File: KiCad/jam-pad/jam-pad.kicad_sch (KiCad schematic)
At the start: 80 parts, among them J1 USB_C, J2 PH_01x03_2.54mm, SW1 MX_Hotswap_LED_RGB, SW13 SW_Push, SW14 RotaryEncoder_Switch, SW15 SW_Push, SW2 MX_Hotswap_LED_RGB, SW3 MX_Hotswap_LED_RGB, SW4 MX_Hotswap_LED_RGB, SW5 MX_Hotswap_LED_RGB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

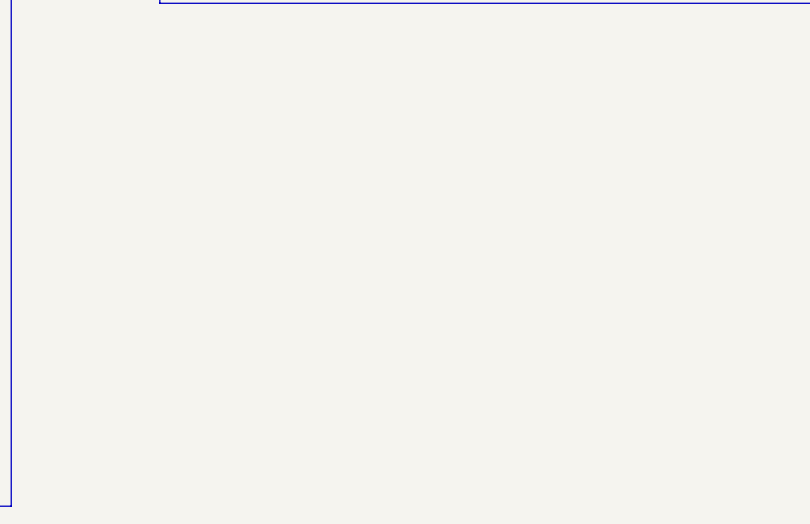
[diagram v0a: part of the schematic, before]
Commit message: Remove unconnected tracks and pass schematic parity
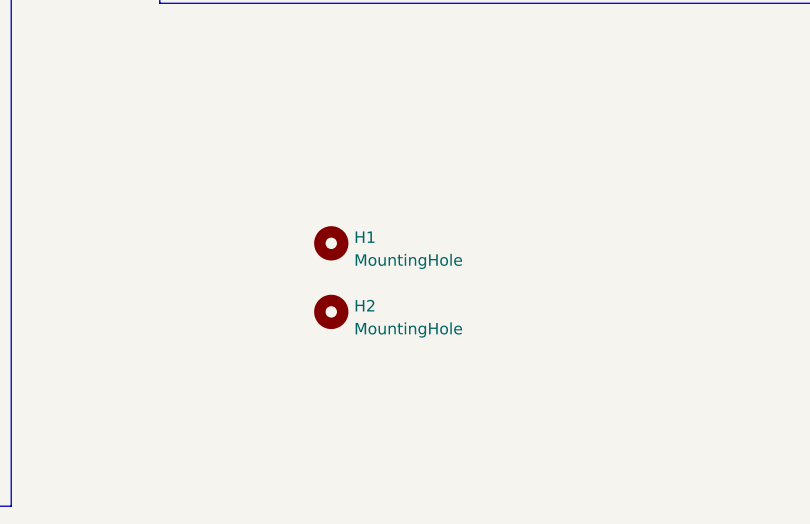
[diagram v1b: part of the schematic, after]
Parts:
- added H1, H2: MountingHole, MountingHole:MountingHole_2.2mm_M2_Pad, symbol Mechanical:MountingHole
- U1: footprint jam-pad:RP2040-QFN-56_HandSoldering -> jam-pad:RP2040-QFN-56
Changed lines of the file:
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@@
       (effects (font (size 1.27 1.27)))
     )
-    (property "Footprint" "jam-pad:RP2040-QFN-56_HandSoldering" (at 322.58 119.38 0)
+    (property "Footprint" "jam-pad:RP2040-QFN-56" (at 322.58 119.38 0)
       (effects (font (size 1.27 1.27)) hide)
     )
@@
     )
   )
+  (symbol (lib_id "Mechanical:MountingHole") (at 284.48 228.6 0) (unit 1)
+    (in_bom no) (on_board yes) (dnp no) (fields_autoplaced)
+    (property "Reference" "H2" (at 287.02 227.965 0)
+      (effects (font (size 1.27 1.27)) (justify left))
+    )
+    (property "Value" "MountingHole" (at 287.02 230.505 0)
+      (effects (font (size 1.27 1.27)) (justify left))
+    )
+    (property "Footprint" "MountingHole:MountingHole_2.2mm_M2_Pad" (at 284.48 228.6 0)
+      (effects (font (size 1.27 1.27)) hide)
+    )
+    (property "Datasheet" "~" (at 284.48 228.6 0)
+      (effects (font (size 1.27 1.27)) hide)
+    )
+    (property "JLCPCB_IGNORE" "Y" (at 284.48 228.6 0)
+      (effects (font (size 1.27 1.27)) hide)
+    )
+    (instances
+      (project "jam-pad"
+        (path "/1926255f-b0ba-44f2-aedc-792e85134e40"
+          (reference "H2") (unit 1)
+        )
+      )
+    )
+  )
   (symbol (lib_id "power:GND") (at 273.05 124.46 270) (unit 1)
     (in_bom yes) (on_board yes) (dnp no)
@@
         )
       )
+    )
+  )
+  (symbol (lib_id "Mechanical:MountingHole") (at 284.48 220.98 0) (unit 1)
+    (in_bom no) (on_board yes) (dnp no) (fields_autoplaced)
+    (property "Reference" "H1" (at 287.02 220.345 0)
+      (effects (font (size 1.27 1.27)) (justify left))
+    )
+    (property "Value" "MountingHole" (at 287.02 222.885 0)
+      (effects (font (size 1.27 1.27)) (justify left))
+    )
+    (property "Footprint" "MountingHole:MountingHole_2.2mm_M2_Pad" (at 284.48 220.98 0)
+      (effects (font (size 1.27 1.27)) hide)
+    )
+    (property "Datasheet" "~" (at 284.48 220.98 0)
+      (effects (font (size 1.27 1.27)) hide)
+    )
+    (property "JLCPCB_IGNORE" "Y" (at 284.48 220.98 0)
+      (effects (font (size 1.27 1.27)) hide)
+    )
+    (instances
+      (project "jam-pad"
+        (path "/1926255f-b0ba-44f2-aedc-792e85134e40"
+          (reference "H1") (unit 1)
+        )
+      )

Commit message: fab, clover logo, some other stuff? idr sorry
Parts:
- SW1, SW2, SW3, SW4, SW5, SW6, SW7, SW8, SW9, Y1: JLCPCB_IGNORE (none) -> Y
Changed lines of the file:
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@@
       (effects (font (size 1.27 1.27)) hide)
     )
+    (property "JLCPCB_IGNORE" "Y" (at 156.21 107.95 0)
+      (effects (font (size 1.27 1.27)) hide)
+    )
     (pin "1")
     (pin "2")
@@
       (effects (font (size 1.27 1.27)) hide)
     )
+    (property "JLCPCB_IGNORE" "Y" (at 156.21 120.65 0)
+      (effects (font (size 1.27 1.27)) hide)
+    )
     (pin "1")
     (pin "2")
@@
       (effects (font (size 1.27 1.27)) hide)
     )
+    (property "JLCPCB_IGNORE" "Y" (at 243.84 144.145 0)
+      (effects (font (size 1.27 1.27)) hide)
+    )
     (pin "1")
     (pin "2")
@@
       (effects (font (size 1.27 1.27)) hide)
     )
+    (property "JLCPCB_IGNORE" "Y" (at 181.61 107.95 0)
+      (effects (font (size 1.27 1.27)) hide)
+    )
     (pin "1")
     (pin "2")
@@
       (effects (font (size 1.27 1.27)) hide)
     )
+    (property "JLCPCB_IGNORE" "Y" (at 167.64 144.145 0)
+      (effects (font (size 1.27 1.27)) hide)
+    )
     (pin "1")
     (pin "2")
@@
       (effects (font (size 1.27 1.27)) hide)
     )
+    (property "JLCPCB_IGNORE" "Y" (at 121.92 144.145 0)
+      (effects (font (size 1.27 1.27)) hide)
+    )
     (pin "1")
     (pin "2")
@@
       (effects (font (size 1.27 1.27)) hide)
     )
+    (property "JLCPCB_IGNORE" "Y" (at 152.4 144.145 0)
+      (effects (font (size 1.27 1.27)) hide)
+    )
     (pin "1")
     (pin "2")
@@
       (effects (font (size 1.27 1.27)) hide)
     )
+    (property "JLCPCB_IGNORE" "Y" (at 181.61 95.25 0)
+      (effects (font (size 1.27 1.27)) hide)
+    )
     (pin "1")
     (pin "2")
@@
       (effects (font (size 1.27 1.27)) hide)
     )
+    (property "JLCPCB_IGNORE" "Y" (at 182.88 144.145 0)
+      (effects (font (size 1.27 1.27)) hide)
+    )
     (pin "1")
     (pin "2")
@@
       (effects (font (size 1.27 1.27)) hide)
     )
+    (property "JLCPCB_IGNORE" "Y" (at 228.6 144.145 0)
+      (effects (font (size 1.27 1.27)) hide)
+    )
     (pin "1")
     (pin "2")
@@
       (effects (font (size 1.27 1.27)) hide)
     )
+    (property "JLCPCB_IGNORE" "Y" (at 213.36 144.145 0)
+      (effects (font (size 1.27 1.27)) hide)
+    )
     (pin "1")
     (pin "2")
@@
       (effects (font (size 1.27 1.27)) hide)
     )
+    (property "JLCPCB_IGNORE" "Y" (at 285.75 124.46 0)
+      (effects (font (size 1.27 1.27)) hide)
+    )
     (pin "1")
     (pin "2")
@@
       (effects (font (size 1.27 1.27)) hide)
     )
+    (property "JLCPCB_IGNORE" "Y" (at 156.21 95.25 0)
+      (effects (font (size 1.27 1.27)) hide)
+    )
     (pin "1")
     (pin "2")
@@
       (effects (font (size 1.27 1.27)) hide)
     )
+    (property "JLCPCB_IGNORE" "Y" (at 198.12 144.145 0)
+      (effects (font (size 1.27 1.27)) hide)
+    )
     (pin "1")
     (pin "2")
@@
       (effects (font (size 1.27 1.27)) hide)
     )
+    (property "JLCPCB_IGNORE" "Y" (at 181.61 120.65 0)
+      (effects (font (size 1.27 1.27)) hide)
+    )
     (pin "1")
     (pin "2")
@@
       (effects (font (size 1.27 1.27)) hide)
     )
+    (property "JLCPCB_IGNORE" "Y" (at 137.16 144.145 0)
+      (effects (font (size 1.27 1.27)) hide)
+    )
     (pin "1")
     (pin "2")
@@
       (effects (font (size 1.27 1.27)) hide)
     )
+    (property "JLCPCB_IGNORE" "Y" (at 207.01 120.65 0)
+      (effects (font (size 1.27 1.27)) hide)
+    )
     (pin "1")
     (pin "2")
@@
       (effects (font (size 1.27 1.27)) hide)
     )
+    (property "JLCPCB_IGNORE" "Y" (at 207.01 95.25 0)
+      (effects (font (size 1.27 1.27)) hide)
+    )
     (pin "1")
     (pin "2")
@@
       (effects (font (size 1.27 1.27)) hide)
     )
+    (property "JLCPCB_IGNORE" "Y" (at 207.01 107.95 0)
+      (effects (font (size 1.27 1.27)) hide)
+    )

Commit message: outdated case, updated pec11
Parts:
- SW14: footprint Keebio-Parts:RotaryEncoder_Alps_EC11E-Switch_Vertical_H20mm -> jam-pad:PEC11
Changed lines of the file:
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@@
       (effects (font (size 1.27 1.27)))
     )
-    (property "Footprint" "Keebio-Parts:RotaryEncoder_Alps_EC11E-Switch_Vertical_H20mm" (at 175.26 158.496 0)
+    (property "Footprint" "jam-pad:PEC11" (at 175.26 158.496 0)
       (effects (font (size 1.27 1.27)) hide)
     )
